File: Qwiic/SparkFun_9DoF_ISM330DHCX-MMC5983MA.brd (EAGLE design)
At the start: 25.4 x 25.4 mm, 75 parts, among them J1 QWIIC_RIGHT_ANGLE, J2 QWIIC_RIGHT_ANGLE, U1 ISM330DHCX, U2 MMC5983MA_QFN16

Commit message: Rolls to version v02
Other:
- board text added: "v02"
- board text removed: "v01"
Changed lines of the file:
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@@
 <wire x1="0" y1="0" x2="25.4" y2="0" width="0.2032" layer="20"/>
 <wire x1="25.4" y1="0" x2="25.4" y2="25.4" width="0.2032" layer="20"/>
-<text x="24.882475" y="13.725525" size="0.8128" layer="16" font="vector" ratio="22" rot="SMR270">v01</text>
+<text x="24.882475" y="13.725525" size="0.8128" layer="16" font="vector" ratio="22" rot="SMR270">v02</text>
 <wire x1="9.236075" y1="15.1876125" x2="11.141075" y2="15.1876125" width="0.254" layer="22"/>
 <wire x1="10.633075" y1="14.6796125" x2="10.633075" y2="15.8226125" width="0.254" layer="22" curve="-180"/>

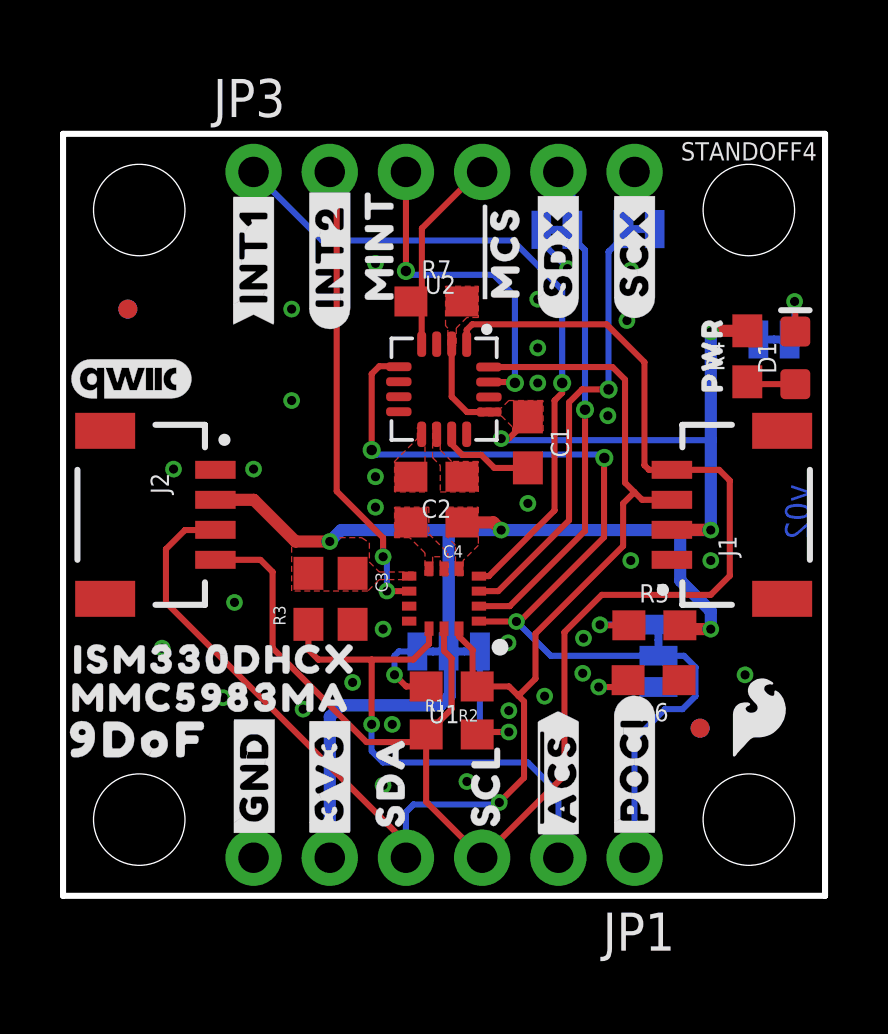
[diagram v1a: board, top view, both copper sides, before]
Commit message: Rotates R7 to make room for silk, nudges R2 to make room for silk
* Fixes some DRC errors
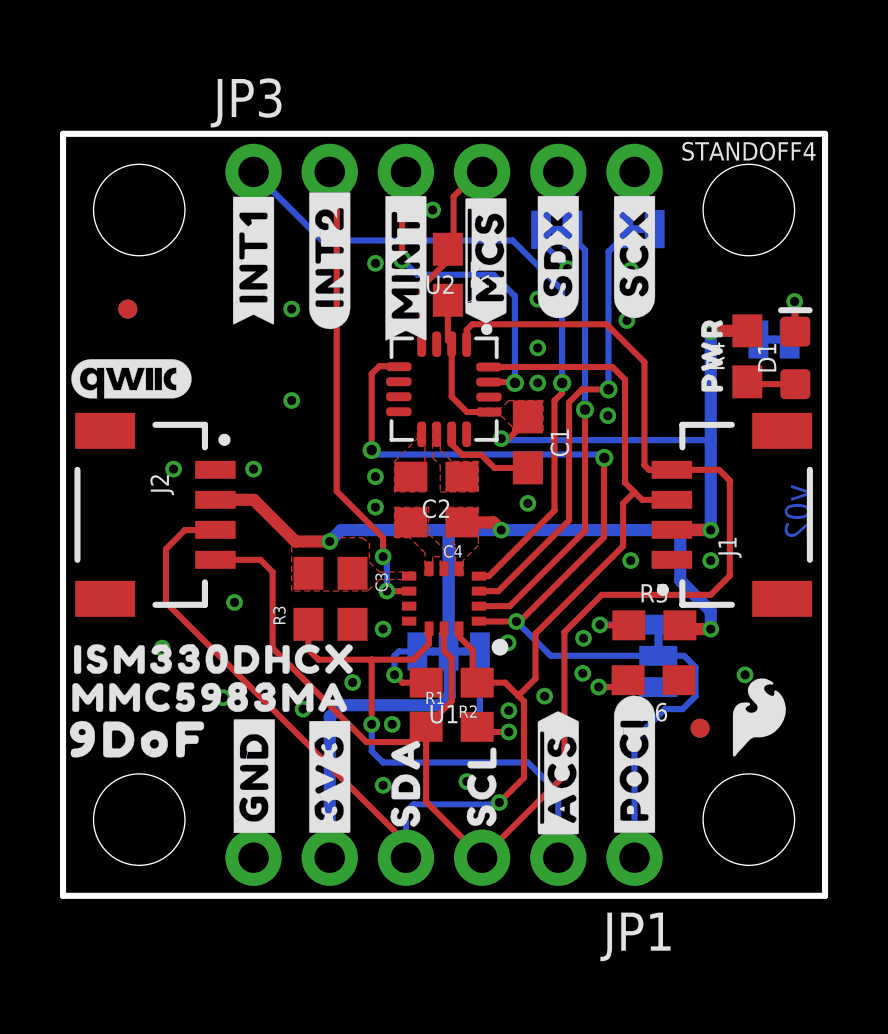
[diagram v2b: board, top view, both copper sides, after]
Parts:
- U$31: device top:MINT3 -> top:#MINT#5
- U$34: device top:#MCS#6 -> top:##MCS##7
- moved U$31 1.09 mm to (11.4, 21.1)
- moved R7 0.97 mm to (12.8, 20.7), turned to 270 degrees
- moved U$34 0.52 mm to (14.1, 21.3)
- moved U$4 0.51 mm to (11.4, 3.81)
- moved R1 0.25 mm to (13.0, 5.63)
- moved R2 0.13 mm to (13.0, 7.11)
- moved U$5 0.13 mm to (14.0, 3.68)
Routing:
- net 3.3V: track 58.6 -> 60.2 mm
- net GND: vias 32 -> 33
